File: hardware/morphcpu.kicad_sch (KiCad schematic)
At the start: 79 parts, among them J1 TYPE-C-31-M-12, SW1 RESET, U1 ICE40UP5K-SG48I, U2 FT231XS-R, U3 W25Q32JVSSIQ, U4 ME6211C33M5G-N, U5 ME6211C12M5G-N, X1 1532H4-16000JWPDTSNL

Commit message: esd array
fixes every discrepancy between docs/BOM.md and the netlist, then pins an LCSC
part number to all 22 BOM rows so a full PCBA quote is possible.

ESD protection. BOM.md and the power tree in DESIGN.md both listed an ESD array
from the start, the schematic never had one. U6 is a USBLC6-2SC6 (C7519,
SOT-23-6) wired into the D+/D- path between J1 and U2. each protected line gets
its own net name either side of the part, USB_DP/USB_DP_F and USB_DM/USB_DM_F,
so the trace routes thru the clamp rather than stubbing off it. placed beside
the connector on the back, the U2-J1 centre line is a 1.2 mm gap, too narrow
for SOT-23-6, and the front is the LED display.

reset switch. the schematic used KiCad's SW_SPST_TL3342 land pattern (6.3 x
3.8 mm pads) but no part was pinned. the switch JLC stocks as Basic is the XKB
TS-1187A at 6.0 x 3.75 mm, close enough to pass a visual check and not close
enough to solder, so the footprint follows the part now.

counts. D17 carried the value "CDONE" and so split into its own BOM row, its
the same KT-0603R as the grid and the value field says so now, giving one LED
row of 17. BOM.md's passive counts were wrong in three places and the schematic
was right every time: 100 nF is 12 not 11, 10k is 9 not 5, and the 1k CDONE
series resistor was missing entirely.

part pinning. all 22 rows carry an LCSC number now, priced at the LCSC
lowest-quantity break. nine of the ten passive values are JLC Basic parts,
confirmed against JLC's category listings. 270R 0402 has no Basic option at JLC
at any tolerance, the alternatives were 300R/330R (changes LED current from
5 mA) or 0603 (changes 16 footprints), neither worth one feeder fee, so it
stays Extended. C7519 and C136491 are listed Extended by inference not by
quote, JLC renders its tier badge in JavaScript and neither part shows up in
the Basic listings. both need confirming in the quote.

component total is $88.06 for 5 boards now, $17.61 per board, every row re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
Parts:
- added U6: USBLC6-2SC6, Package_TO_SOT_SMD:SOT-23-6, symbol Power_Protection:USBLC6-2SC6
- D17: value CDONE -> KT-0603R
- SW1: value RESET -> TS-1187A-B-A-B; footprint Button_Switch_SMD:SW_SPST_TL3342 -> Button_Switch_SMD:SW_Push_1P1T_XKB_TS-1187A
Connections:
- net GND: now also U6.2 (GND)
- net USB_DM: now also U6.1 (I/O1); no longer U2.12 (USBDM)
- net USB_DP: now also U6.3 (I/O2); no longer U2.11 (USBDP)
- net VBUS: now also U6.5 (VBUS)
- new net USB_DM_F: U2.12 (USBDM), U6.6 (I/O1)
- new net USB_DP_F: U2.11 (USBDP), U6.4 (I/O2)
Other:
- moved on the sheet: C1, C10, C11, C12, C13, C14, C15, C16, C17, C18, C19, C2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

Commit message: resistor ring pairing
still 0 tracks and 0 zones. both fixes are in the generators, not hand edits.

LED anode ratsnest 405.0 mm -> 53.4 mm.

  total anode ratsnest        405.0 mm  ->  53.4 mm
  longest single anode    31.7 (LED15_A) ->  5.21 (LED5_A, LED9_A)
  shortest                     17.7 mm  ->  1.49 mm
  chords within 5mm of centre       16  ->  0
  closest approach to centre   0.13 mm  ->  5.83 mm

gen_pcb.py sorted the LEDs by angle correctly then handed out ring slots at
k*22.5 starting from zero. the sorted list starts at -161.6 deg, so every
resistor landed 157-180 deg from its own LED and all 16 anodes ran as chords
under the QFN paddle. the sort was never the problem, the handout was.

a rotation wouldnt have fixed it either. a 4x4 grid on 9mm pitch puts the four
inner LEDs and the four corner LEDs on the same four diagonals, so eight parts
want four rays. each resistor now sits on its own LEDs ray, twelve at r=11.5
and the four corner ones at r=14.5 to break the tie. closest pair is 3.00 mm.

LED grid did NOT move. all 16 still at exact 9mm pitch, cell 0 top-left
row-major, front layer, D(n+1) still carrying LED(n)_A. verified pad by pad.

DRC after: 1 violation, a cosmetic C20/R27 silk overlap, plus the expected 167
unconnected. was 3 violations before. zero courtyard overlaps, zero shorting
pads, zero clearance errors, nothing new anywhere near the paddle.

UART off pins 6/9 onto 34/36. UART_TX_O 20.95 -> 13.99 mm, UART_RX_I
26.17 -> 19.16 mm, and neither crosses the board any more. bank 0 is the same
+3V3 VCCIO, no GBIN pin spent, no LED pin touched, no LED bank balance change.
ERC 0 errors 0 warnings.

not zero tradeoffs though: pin 35 (CLK) had empty pads either side and now sits
between two UART nets, so CLK needs a via to the front to turn west instead of
an open channel. written up in ROUTING.md, its one via over a ground pour.

34 is TX and 36 is RX, flipped vs the literal 6->34 9->36 reading. U2 pad 4 is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
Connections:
- net UART_RX_I: now also U1.36 (IOT_48b); no longer U1.6 (IOB_13b)
- net UART_TX_O: now also U1.34 (IOT_44b); no longer U1.9 (IOB_16a)

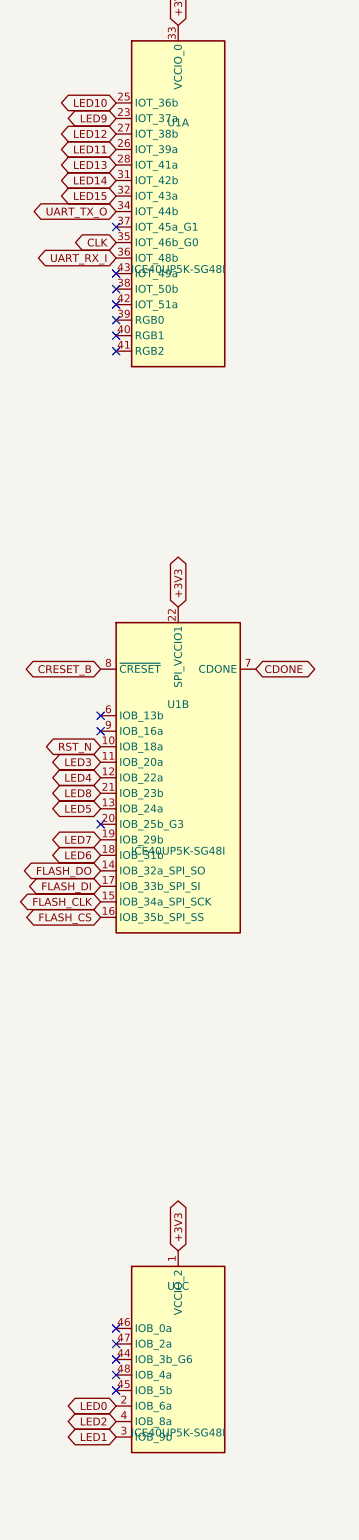
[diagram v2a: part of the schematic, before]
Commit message: fanout was full / six leds onto the south row
U1's east column was carrying twelve nets on twelve 0.5 mm channels and four of
them land on the far side of the board so they cross the fan twice. +3V3 at 22
and 33, +1V2 at 5 and 30, and LED12 had no escape at all

a 0.6 mm via wants 1.2 mm between its neighbours and adjacent escape rays are
0.5 mm apart, so nothing changes layer until the fan has spread. the staggered
two row via fanout fails the same way, the outer neck needs 1.2 mm between two
inner vias and has 1.0 mm. tested that

pads 37-48 were sitting unused. LED12 27->48, LED13 28->46, LED14 31->38,
LED2 4->23, LED3 11->27, ordered by their resistors x so none of them cross.
46/47/48 are bank 2 and 23/27/38 are bank 0, both already +3V3 so no level
change. nothing lands on a config pin, an RGB driver or a global buffer, 20 (G3)
stays free, CLK stays on 35. bank balance 15/30/35 mA -> 25/25/30

LED12/13/14 went 42.0 / 36.1 mm and unroutable to 12.5 / 7.8 / 8.0 mm and eleven
of the twelve outstanding connections then routed with nothing ripped up

four router bugs fixed on the way, each throwing away channels that were legal.
fill_poly rasterising cells as half open squares while cell()/pos() used lattice
points, 0.025 mm off. obstacles inflated by clearance + 0.01 mm when the tightest
real clearances here are 0.2019 mm against a 0.2 mm rule. hole to hole checks
reading ripped up vias off the board's original track list. a route's own vias
never checked against each other, two layer changes in neighbouring cells puts
two holes 0.07 mm apart

netlist.py, morphcpu.pcf and the DESIGN.md pin table moved together, ERC 0/0
after regenerating. VBUS_IN widened to its 0.5 mm class width. USB_DP/DM and
CC1/CC2 untouched, byte identical widths and lengths

0 violations, 7 unconnected -> 0 violations, 3 unconnected
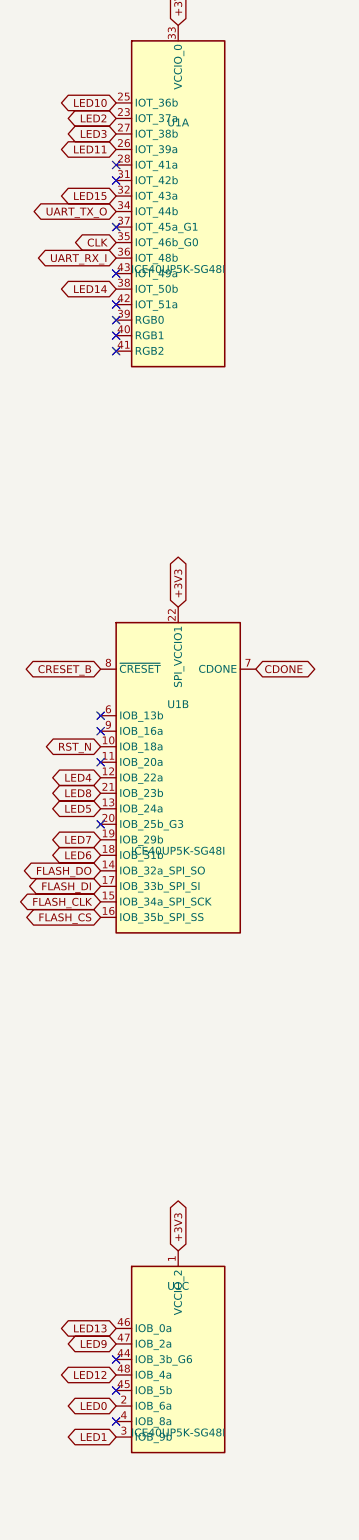
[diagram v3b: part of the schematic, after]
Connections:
- net LED12: now also U1.48 (IOB_4a); no longer U1.27 (IOT_38b)
- net LED13: now also U1.46 (IOB_0a); no longer U1.28 (IOT_41a)
- net LED14: now also U1.38 (IOT_50b); no longer U1.31 (IOT_42b)
- net LED2: now also U1.23 (IOT_37a); no longer U1.4 (IOB_8a)
- net LED3: now also U1.27 (IOT_38b); no longer U1.11 (IOB_20a)
- net LED9: now also U1.47 (IOB_2a); no longer U1.23 (IOT_37a)

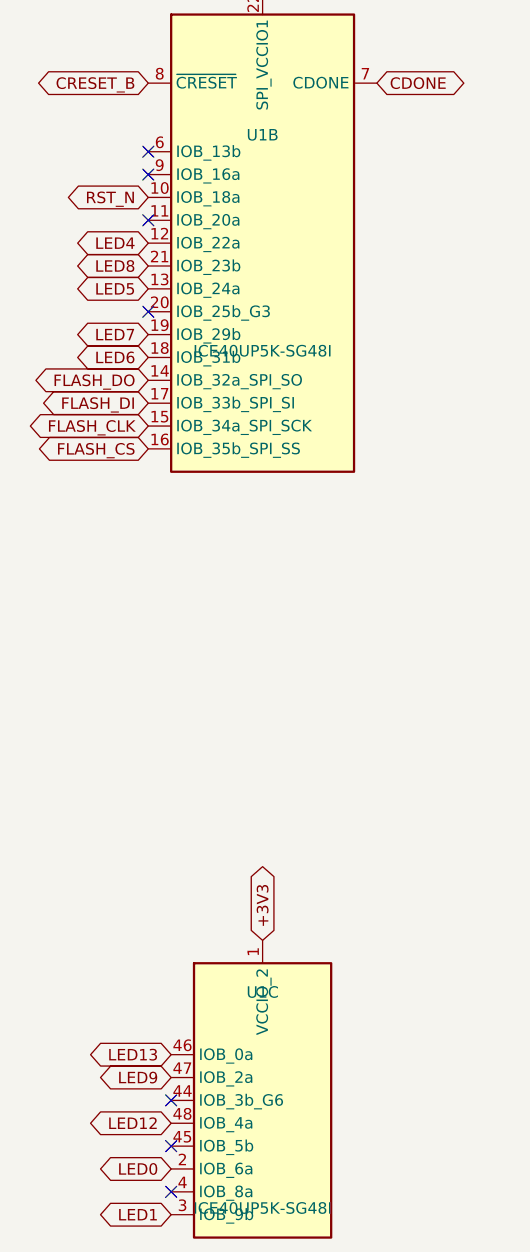
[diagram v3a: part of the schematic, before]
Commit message: led9 onto pin 9 / +1V2 gets out of U1.5
LED9 went to the south row with LED12/13/14 last commit and then spent its time
fighting LED12 on pad 48 for the same southwest corridor. R10 is at 141.5, 108.5
and pad 9's ray on the west face points straight at it, so it goes there and pad
47 is unused again

that frees the west corridor and +1V2 at U1.5 routes. pin 5 is a core VCC pin so
it was the only open connection that actually mattered

left is LED1 (U1.3 -> R2.1) and LED2 (U1.23 -> R3.1). both route alone, never
together. seven pin assignments trialled with +1V2 placed first and every one
lands on two open, just a different two, table is in ROUTING.md

netlist.py, morphcpu.pcf and the DESIGN.md pin table moved together. ERC 0,
board and regenerated schematic agree on every unconnected U1 pad

0 violations, 3 unconnected -> 0 violations, 2 unconnected
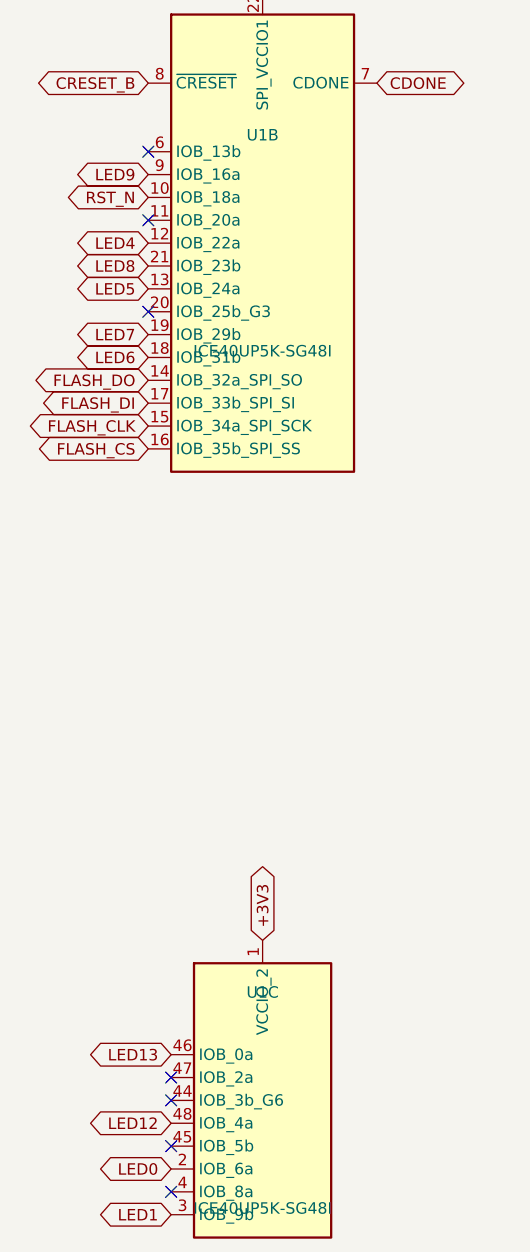
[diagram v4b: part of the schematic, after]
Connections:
- net LED9: now also U1.9 (IOB_16a); no longer U1.47 (IOB_2a)
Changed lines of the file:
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@@
+		(effects (font (size 1.27 1.27)) (justify right))
+	)
+	(global_label "LED9"
+		(shape bidirectional)
+		(at 57.15 142.24 180)
 		(effects (font (size 1.27 1.27)) (justify right))
 	)
@@
 		(shape bidirectional)
 		(at 59.69 240.03 180)
-		(effects (font (size 1.27 1.27)) (justify right))
-	)
-	(global_label "LED9"
-		(shape bidirectional)
-		(at 59.69 242.57 180)
 		(effects (font (size 1.27 1.27)) (justify right))
 	)
@@
 	(no_connect (at 59.69 67.31))
 	(no_connect (at 57.15 139.7))
-	(no_connect (at 57.15 142.24))
 	(no_connect (at 57.15 147.32))
 	(no_connect (at 57.15 157.48))
@@
 	(no_connect (at 59.69 245.11))
 	(no_connect (at 59.69 250.19))
+	(no_connect (at 59.69 242.57))
 	(no_connect (at 302.26 54.61))
 	(no_connect (at 302.26 49.53))
